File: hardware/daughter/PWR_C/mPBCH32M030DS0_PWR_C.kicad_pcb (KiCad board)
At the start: 2 copper layers, 22.9 x 70.7 mm, 71 parts, among them J1 SOCK_L, J2 SOCK_R, J3 PWR_IN, J4 MOTOR, Q1 MTN2306AN3, Q10 TPN1R603PL, Q2 MTN2306AN3, Q3 MTN2306AN3, Q4 MTN2306AN3, Q5 MTN2306AN3, Q6 MTN2306AN3, Q7 MTN2306AN3, Q8 MTN2306AN3, Q9 TPN2R304PL, U2 78L05, U4 LM74700-Q1, U5 LM74700-Q1

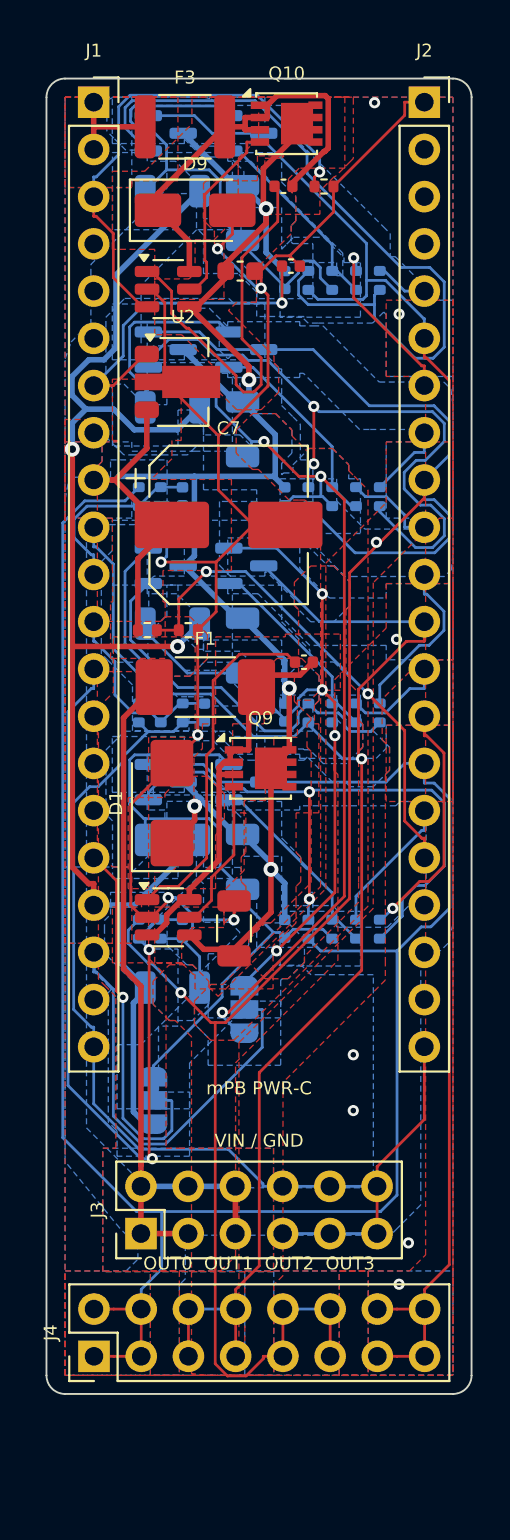
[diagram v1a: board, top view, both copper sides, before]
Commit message: 子基板 A/C: 電源の銅箔を配線前に置く再レイアウト (A 約4A/相, C 3A)
- レッグを LS/HS の縦ブロックにし, 下面 = ISH の背骨 + SRC/VBUS/SW の島,
  上面 = VBUS の帯と各相 SW の階段状の帯 (J4 は 180° 回転: OUT3 が上)
- 固定ベタは DSN では keepout (縁 0.3mm は同ネットの取り付き用) + via_keepout にして
  自動配線がベタを削らないようにした。2 段配線 (MPB_TWO_PHASE) も用意
- A: ゲート抵抗 (0805) の電極間を SW/GL が抜ける配置 (J2 の並びと FET のゲート位置の上下逆を解消)
- A/C: バルク容量は ISH 戻り (VBUS-ISH), USB 側 TVS (D9) は省略, NTC は下側へ
- 電流チェックに 1mm 平均の密度 (角の電流集中を除く) を追加
- ヒートシンクの干渉チェックは MOSFET の範囲だけに

Co-Authored-By: Claude Opus 5.5 <noreply@anthropic.com>
Claude-Session: https://claude.ai/code/session_01LENFjjhDfYjJZV1NWhB9uV
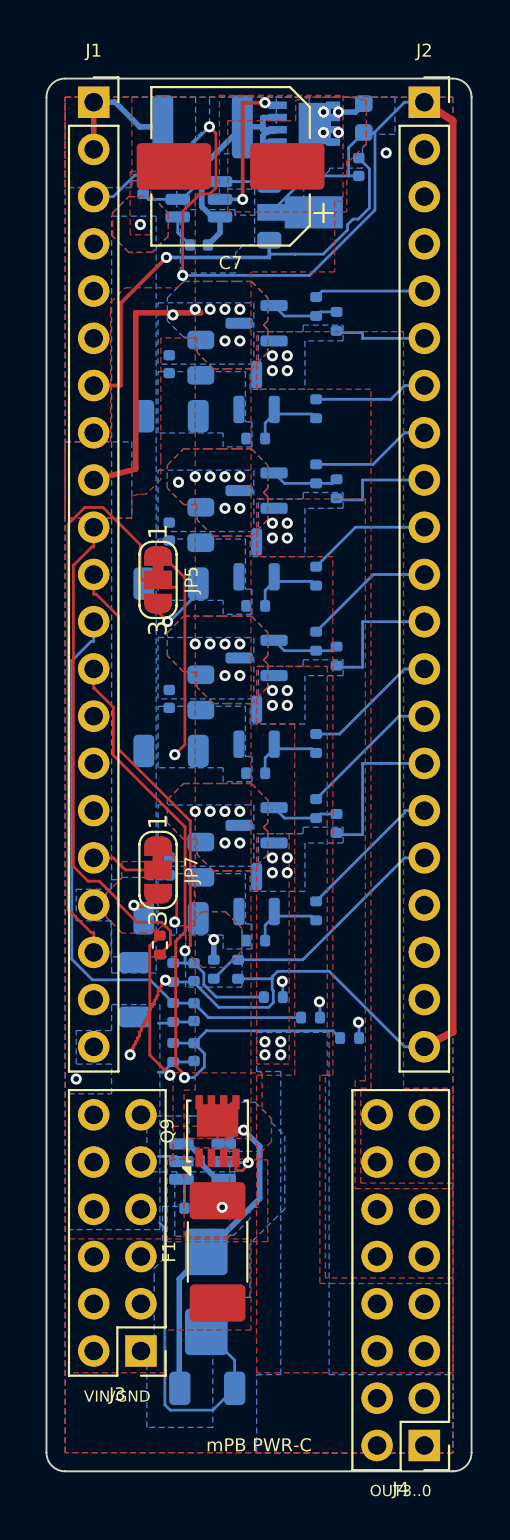
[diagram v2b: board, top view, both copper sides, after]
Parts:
- removed D9: SMAJ20A, D_SMA
- C1, C3, C4, C5, C6, D1, F3, Q10, R11, R12, R6, U2, U4, U5: moved to B.Cu
- C31, C41, C51, C61: value 10uF/50V -> 10uF/25V; footprint C_1206_3216Metric -> C_0805_2012Metric
- F1: value 10A -> 5A
- JP5, JP7, TH1: moved to F.Cu
- moved F1 30.4 mm to (9.20, 63.1), turned to 90 degrees
- moved C5 30.0 mm to (7.90, 60.8)
- moved R71 27.9 mm to (12.2, 49.4), turned to 180 degrees
- moved D1 26.4 mm to (8.59, 65.2), turned to -90 degrees
- moved R72 25.6 mm to (6.81, 48.1)
- moved C71 25.6 mm to (7.93, 48.1)
- moved C1 24.8 mm to (8.64, 70.4), turned to 0 degrees
- moved JP5 23.6 mm to (6.00, 27.0)
- moved Q9 19.6 mm to (9.20, 56.6), turned to 90 degrees
- moved C7 19.3 mm to (9.90, 4.72), turned to 180 degrees
- moved R11 18.6 mm to (9.00, 47.9), turned to -90 degrees
- moved R12 18.4 mm to (10.3, 47.9), turned to -90 degrees
- moved J4 18.4 mm to (20.3, 73.5), turned to 180 degrees
- moved R74 18.3 mm to (14.2, 50.5), turned to 180 degrees
- moved C72 16.1 mm to (7.93, 50.2)
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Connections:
- C7 pad 2: GND -> ISH
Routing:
- net SW0: track 117.5 -> 9.31 mm, vias 0 -> 9
- net SW2: track 107.4 -> 6.55 mm, vias 2 -> 5
- net SW3: track 87.1 -> 4.93 mm, vias 2 -> 4
- net ISH: track 77.9 -> 1.55 mm
- net SW1: track 82.0 -> 7.93 mm, vias 2 -> 5
- net VBUS: track 110.9 -> 41.3 mm, vias 5 -> 32
- net SRC2: track 61.3 -> 3.00 mm, vias 3 -> 1
- net VIN: track 40.6 -> 0.00 mm
- net GH3: track 40.7 -> 3.69 mm
- net GH2: track 36.4 -> 3.69 mm, vias 2 -> 0
- net SRC1: track 43.2 -> 11.7 mm, vias 4 -> 1
- net SRC0: track 35.4 -> 4.71 mm, vias 0 -> 1
- net GH0: track 33.4 -> 3.69 mm, vias 2 -> 0
- net SRC3: track 26.3 -> 0.00 mm
- net BEMF_V: track 10.3 -> 32.3 mm
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- added copper zone on B.Cu, net USB_VBUS_P
- added copper zone on B.Cu, net VIN_F
- removed copper zone on F.Cu, net SRC1
- removed copper zone on F.Cu, net SRC2
- removed copper zone on F.Cu, net USB_VBUS_P
- removed copper zone on B.Cu, net VIN
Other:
- board size 22.9 x 70.7 mm -> 22.9 x 74.9 mm
- board text added: "OUT3..0"
- board text added: "VIN/GND"
- board text removed: "OUT0 OUT1 OUT2 OUT3"
- board text removed: "VIN / GND"

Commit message: 子基板 A/C: 電源ベタにはんだ盛り用のレジスト開口, JP5 の向きを修正
- 配線前に置く電源ベタ (VBUS/ISH/VIN/VIN_F/GND/SW*/SRC*) の上のレジストを開ける
  (ベタの塗りを 0.25mm 内側に縮めた形。銅の縁と他ネットの間はレジストを残してブリッジを防ぐ)
- JP5 を 180° 回して 1 番 (SRC1) をレッグ 1 側へ。SRC2 が ISH の背骨 (下面) を横切っていたのを解消
  (A の ISH レッグ 2/3: 4.5A → 7.9A)
- 電流容量チェック (tools/power_check): レジスト開口のはんだ厚 (MPB_SOLDER_T) を銅の厚みに換算して解く
- A: はんだ 0.3mm 盛りで全経路 5A 以上 (最小 SW 5.9A, USB 系 3A 経路 5.1A 以上)
- C: 全経路 3A 以上 (USB 帰路 GND が 3.0A で最小)

Co-Authored-By: Claude Opus 5.5 <noreply@anthropic.com>
Claude-Session: https://claude.ai/code/session_01LENFjjhDfYjJZV1NWhB9uV
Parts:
- turned JP5 to 90 degrees
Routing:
- net GND: track 152.9 -> 127.3 mm
- net BEMF_V: track 32.3 -> 43.2 mm, vias 0 -> 1
- net BEMF_W: track 36.7 -> 41.3 mm
- net BEMF_U: track 29.2 -> 33.4 mm, vias 1 -> 0
- net SRC1: track 11.7 -> 8.47 mm
- net SRC2: track 3.00 -> 4.48 mm
- net NTC: track 27.0 -> 25.6 mm
- net VBUS: track 41.3 -> 41.0 mm, vias 32 -> 33
